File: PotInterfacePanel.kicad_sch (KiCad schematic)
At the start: 30 parts, among them J5 Led, J6 Conn_01x02_Socket, J7 Conn_02x05_Odd_Even, Q1 BC547, Q2 BC547, U1 SM420561N, U2 ATmega328P-P, U4 SM420561N, Y1 Crystal

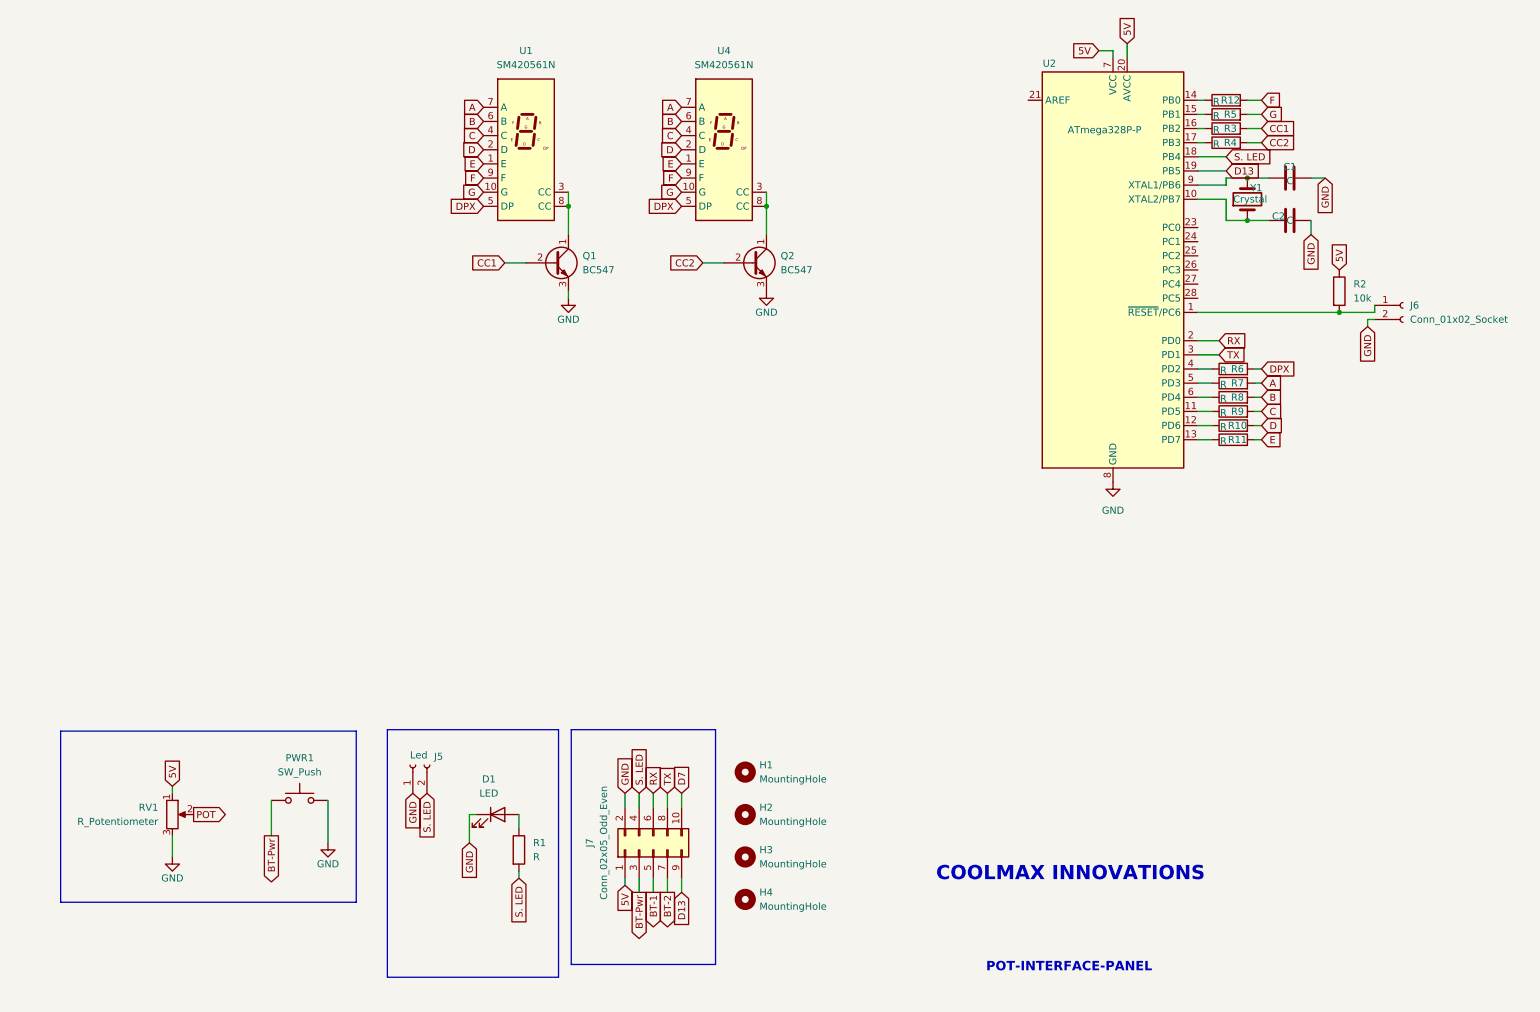
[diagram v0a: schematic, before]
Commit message: 14seg-Display with a Potentiometer Knob
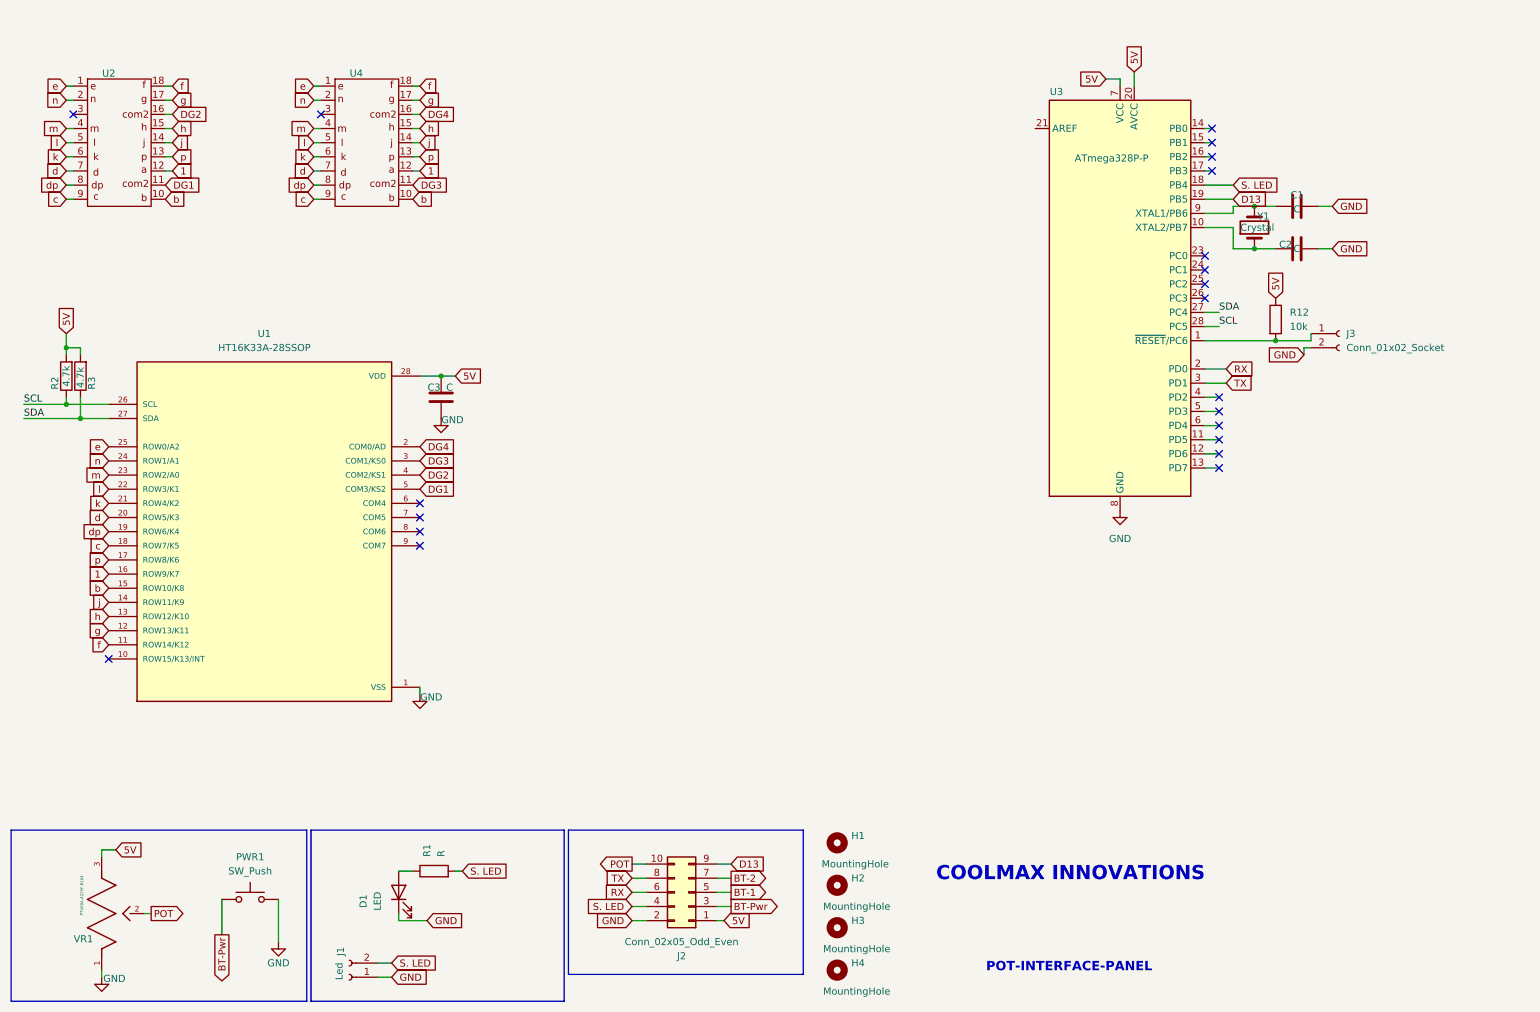
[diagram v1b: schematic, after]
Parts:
- removed Q1, Q2: BC547, Package_TO_SOT_THT:TO-92_Inline, symbol Transistor_BJT:BC547
- removed R10, R11, R12, R4, R5, R6, R7, R8, R9: R, Resistor_THT:R_Axial_DIN0204_L3.6mm_D1.6mm_P5.08mm_Horizontal, symbol Device:R
- removed RV1: R_Potentiometer, symbol Device:R_Potentiometer
- removed U1, U4: SM420561N, Display_7Segment:7SegmentLED_LTS6760_LTS6780, symbol Display_Character:SM420561N
- added C3: C, Capacitor_THT:C_Disc_D3.0mm_W1.6mm_P2.50mm, symbol Device:C
- added R2: 4.7k, Resistor_THT:R_Axial_DIN0204_L3.6mm_D1.6mm_P5.08mm_Horizontal, symbol Device:R
- added U1: HT16K33A-28SSOP, ht16k33A-28ssop:SOP63P600X175-28N, symbol ht16k33-28ssop:HT16K33A-28SSOP
- added U2, U4: ~, custom_footprint:14seg, symbol custom_symbols:14seg
- added VR1: PTV09A-4225F-B104, pot:PTV09, symbol pot:PTV09A-4225F-B104
- R3: value R -> 4.7k
- renumbered J5 to J1, J7 to J2, J6 to J3, R2 to R12, U2 to U3
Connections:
- net CC1 is gone; now on net 5V: R3.2
- net D7 is gone; now on net POT: J2.10 (Pin_10)
- net 5V: now also C3.2, R2.2, U1.28 (VDD), VR1.3
- net GND: now also C3.1, U1.1 (VSS), VR1.1
- net POT: now also VR1.2
- net at U3.16 (PB2): no longer R3.1
- net SDA: now reaches U3.27 (PC4)
- net SDA: now also R3.1, U1.27 (SDA)
- net SCL: now reaches U3.28 (PC5)
- net SCL: now also R2.1, U1.26 (SCL)
- new net 1: U1.16 (ROW9/K7), U2.12, U4.12
- new net DG1: U1.5 (COM3/KS2), U2.11
- new net DG2: U1.4 (COM2/KS1), U2.16
- new net DG3: U1.3 (COM1/KS0), U4.11
- new net DG4: U1.2 (COM0/AD), U4.16
- new net b: U1.15 (ROW10/K8), U2.10, U4.10
- new net c: U1.18 (ROW7/K5), U2.9, U4.9
- new net d: U1.20 (ROW5/K3), U2.7, U4.7
- new net dp: U1.19 (ROW6/K4), U2.8, U4.8
- new net e: U1.25 (ROW0/A2), U2.1, U4.1
- new net f: U1.11 (ROW14/K12), U2.18, U4.18
- new net g: U1.12 (ROW13/K11), U2.17, U4.17
- new net h: U1.13 (ROW12/K10), U2.15, U4.15
- new net j: U1.14 (ROW11/K9), U2.14, U4.14
- new net k: U1.21 (ROW4/K2), U2.6, U4.6
- new net l: U1.22 (ROW3/K1), U2.5, U4.5
- new net m: U1.23 (ROW2/A0), U2.4, U4.4
- new net n: U1.24 (ROW1/A1), U2.2, U4.2
- new net p: U1.17 (ROW8/K6), U2.13, U4.13
- no-connect marks 0 -> 21
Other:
- moved on the sheet: C1, C2, D1, H1, H2, H3, H4, J1, J2, J3, PWR1, R1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

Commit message: 3dfiles
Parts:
- C3: footprint Capacitor_THT:C_Disc_D3.0mm_W1.6mm_P2.50mm -> Capacitor_SMD:C_1206_3216Metric
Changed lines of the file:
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@@
 			)
 		)
-		(property "Footprint" "Capacitor_THT:C_Disc_D3.0mm_W1.6mm_P2.50mm"
+		(property "Footprint" "Capacitor_SMD:C_1206_3216Metric"
 			(at 91.7448 83.82 0)
 			(effects
